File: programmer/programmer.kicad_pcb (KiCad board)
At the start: 2 copper layers, 48 x 48 mm, 1 part

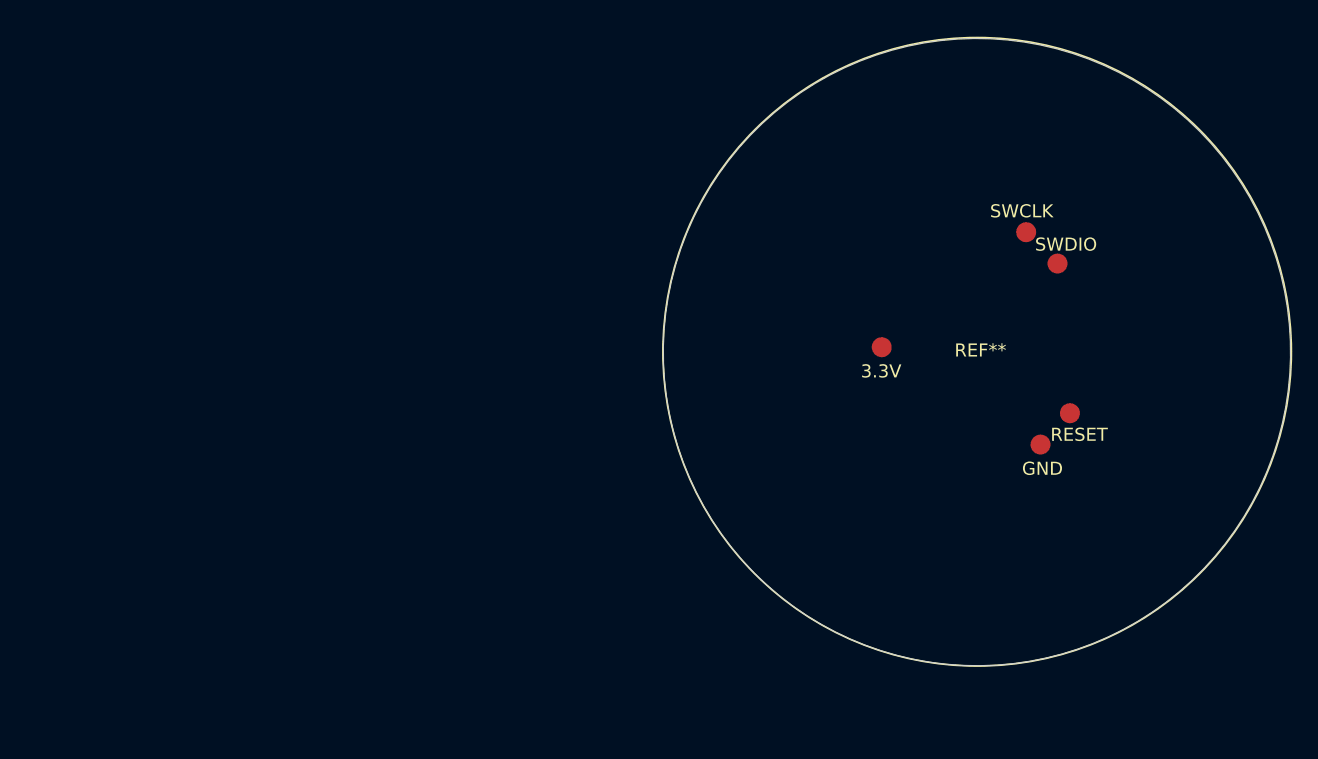
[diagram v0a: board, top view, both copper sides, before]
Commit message: first complete pass at a programmer pcb & accompanying 3d-printable caddy; create footprints for programmer pins including the first fab run as well as a new design for v2 programmer pins
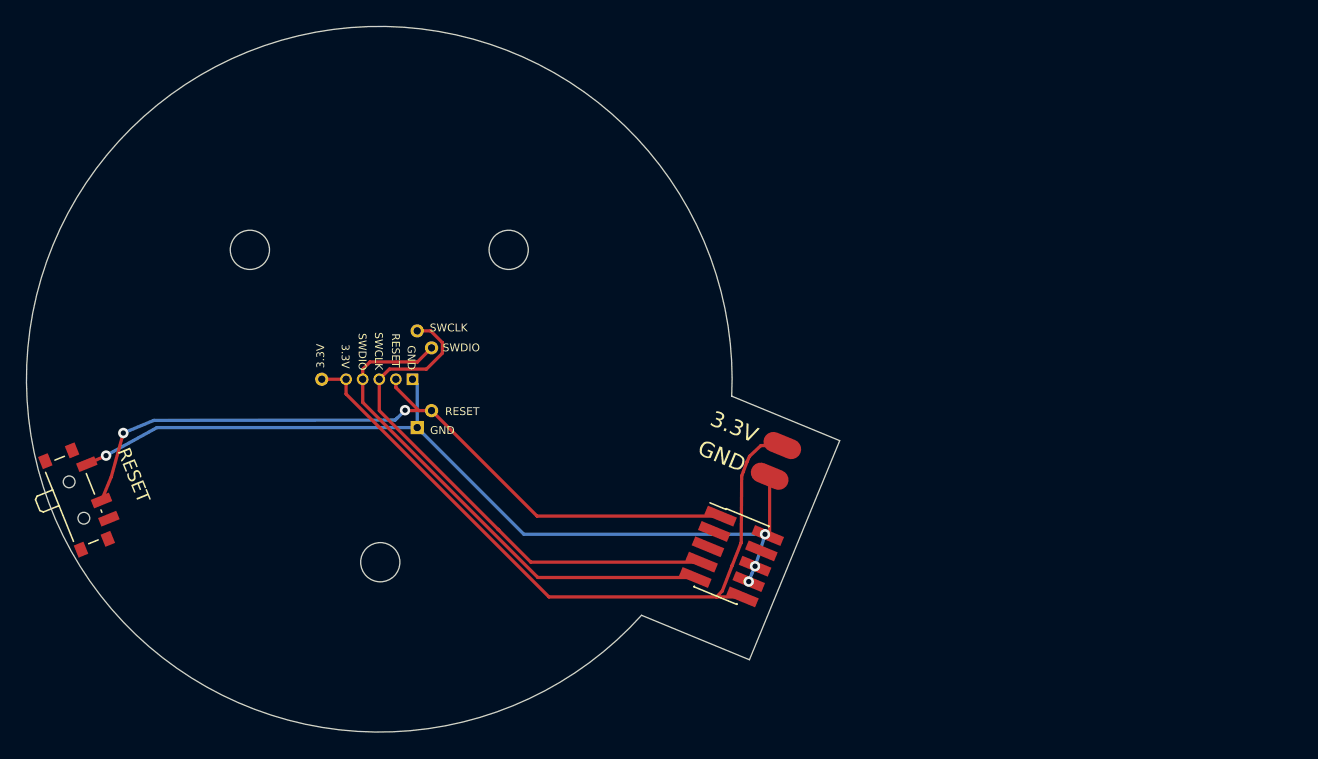
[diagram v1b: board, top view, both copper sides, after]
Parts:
- removed REF**: earthvenusmars_programmer, earthvenusmars:programmer
- added J1: v1 programmer, earthvenusmars:programmer_pins_v1, F.Cu at (100.0, 100.0)
- added J2: v2 programmer, earthvenusmars:programmer_pins_v2, F.Cu at (100.0, 100.0)
- added JLINK1: Conn_02x05_Top_Bottom, Connector_PinHeader_1.27mm:PinHeader_2x05_P1.27mm_Vertical_SMD, F.Cu at (126.9, 113.6)
- added JP1: Conn_01x02_Female, Pad_SMD:Pad_SMD_01x02, F.Cu at (130.4, 106.2)
- added RESET: SW_SPST, Button_Switch_SMD:SW_SPDT_PCM12, F.Cu at (77.1, 109.1)
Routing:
- net GND: track 0.00 -> 69.1 mm, vias 0 -> 4
- net /RESET: track 0.00 -> 58.1 mm, vias 0 -> 2
- net +3V3: track 0.00 -> 53.9 mm
- net /SWCLK: track 0.00 -> 40.8 mm
- net /SWDIO: track 0.00 -> 39.5 mm
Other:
- board size 48 x 48 mm -> 62.2 x 54 mm
- board text added: "3.3V"
- board text added: "GND"

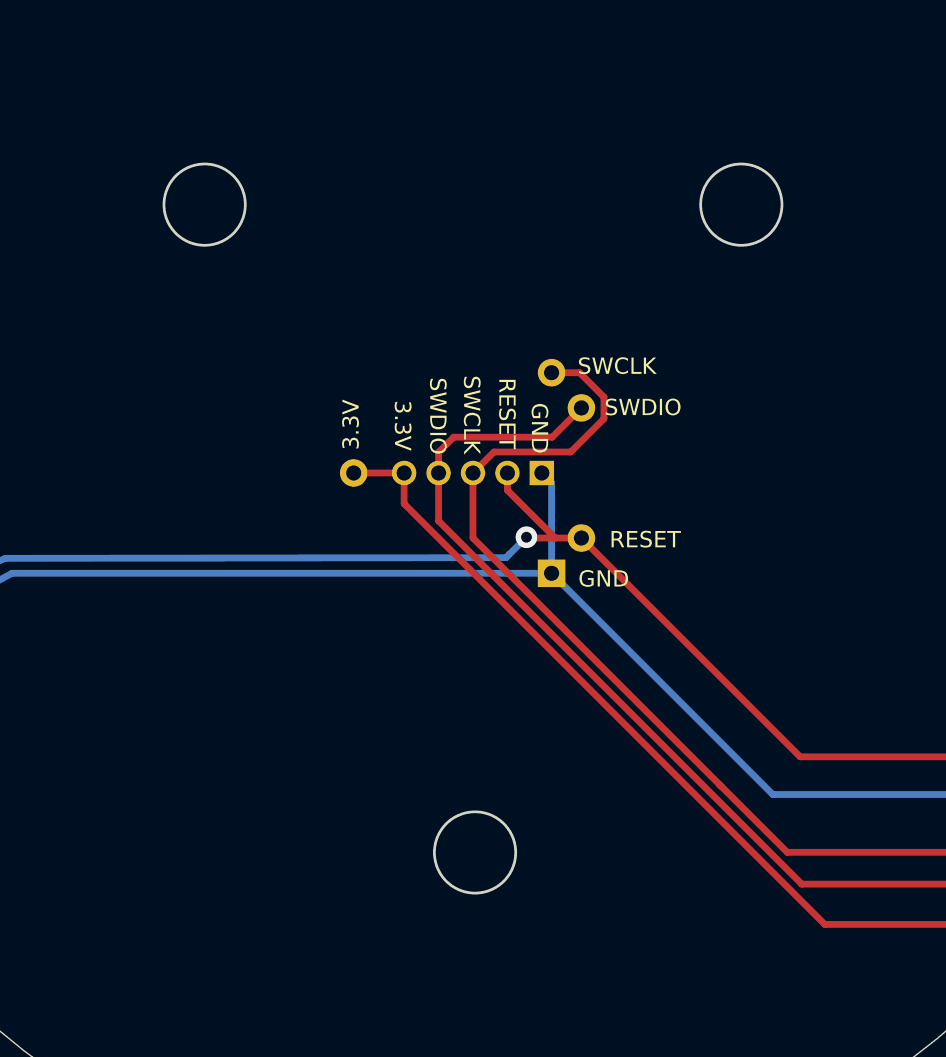
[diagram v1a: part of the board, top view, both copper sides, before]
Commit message: change screw drill size to 1.25mm for M3 screws (which apparently have 3mm major dimension and expect a 2.5mm drill)
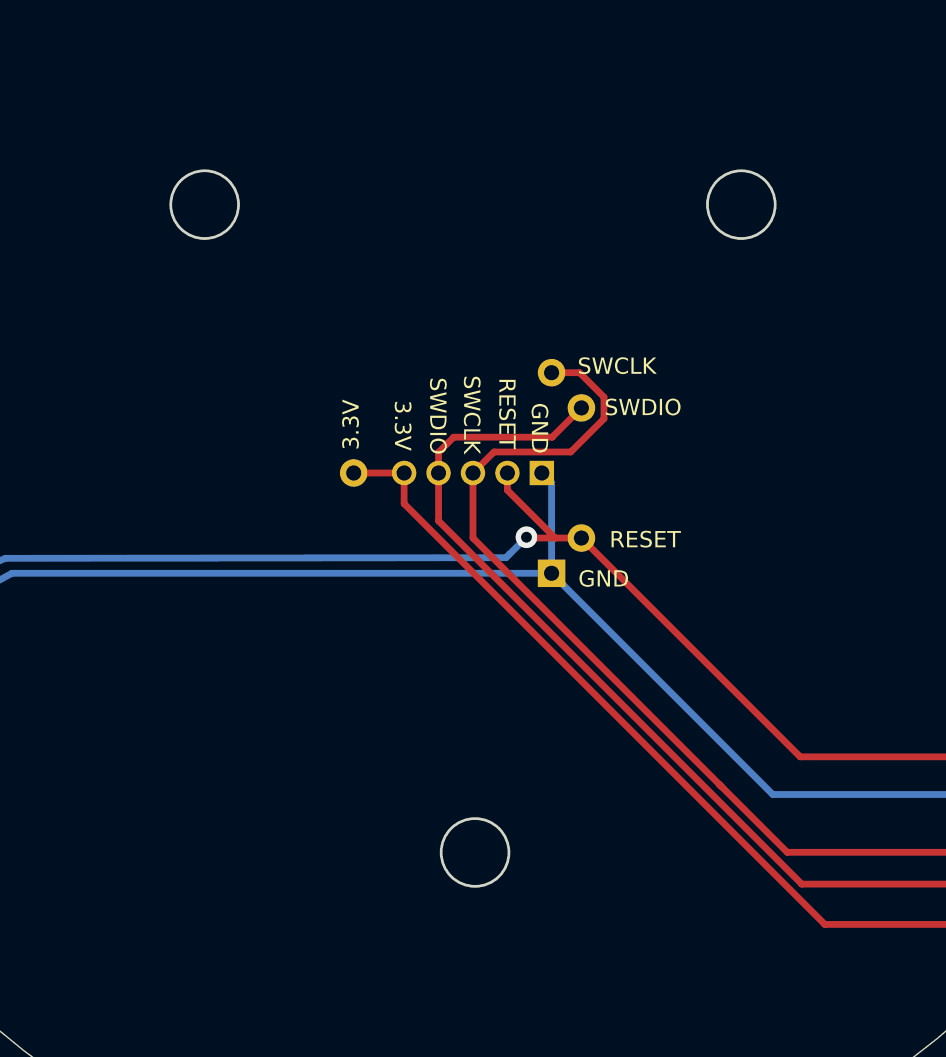
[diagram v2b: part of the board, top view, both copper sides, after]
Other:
- outline, holes or cut-outs redrawn

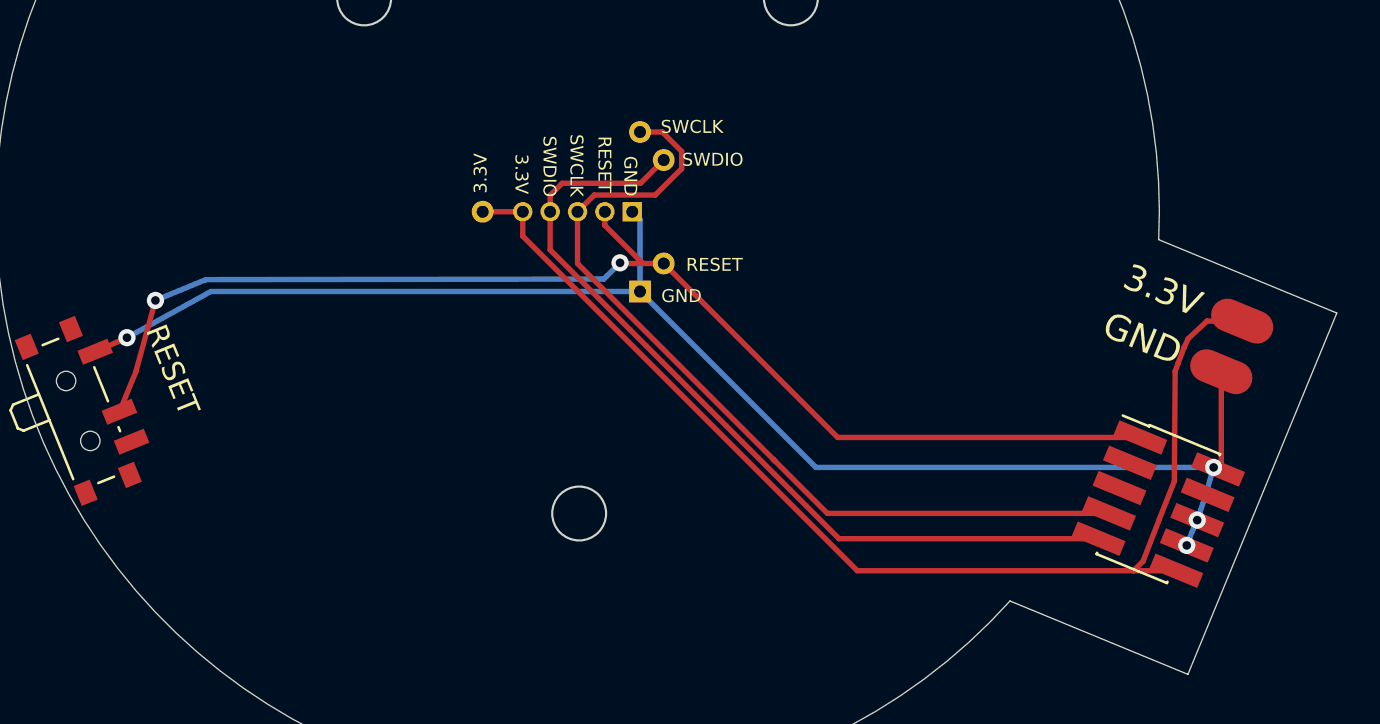
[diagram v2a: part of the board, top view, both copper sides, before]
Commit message: correct footprint for SMD SWD socket (part 3221-10-0300-00 ordered from digikey)
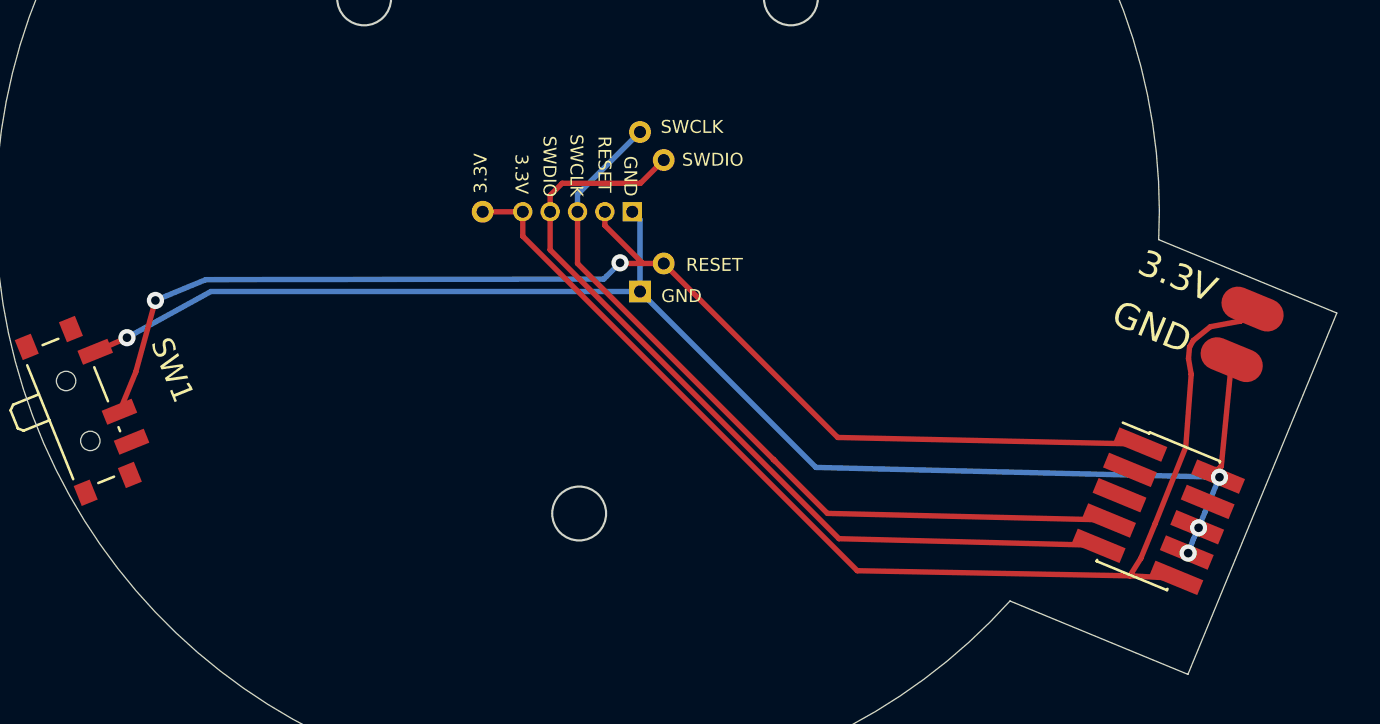
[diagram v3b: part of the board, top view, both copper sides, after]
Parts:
- moved JP1 0.74 mm to (130.8, 105.7)
- moved SWD1 0.33 mm to (126.9, 113.9)
- renumbered RESET to SW1, JLINK1 to SWD1
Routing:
- net /SWCLK: track 40.8 -> 36.8 mm
- net GND: track 69.1 -> 70.2 mm
- net +3V3: track 53.9 -> 54.6 mm
